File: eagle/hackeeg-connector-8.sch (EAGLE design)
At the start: 19 parts

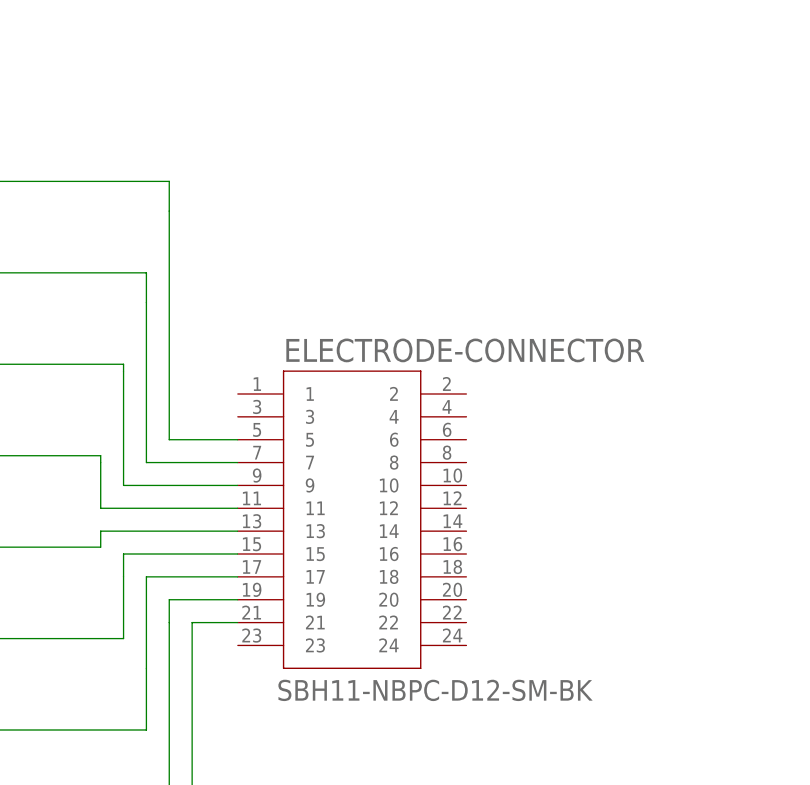
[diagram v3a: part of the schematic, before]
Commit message: connected IN1-8N to AGND
- for cable noise reduction
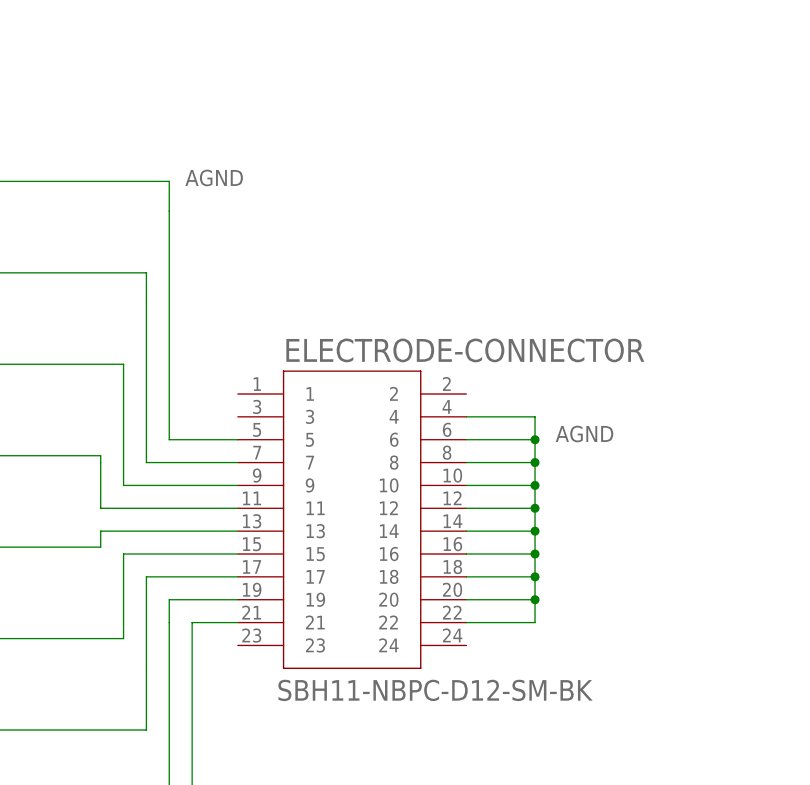
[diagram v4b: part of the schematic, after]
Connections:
- removed net N$1: AGND.SIGNAL, ELECTRODE-CONNECTOR.5
- new net AGND: AGND.SIGNAL, ELECTRODE-CONNECTOR.10, ELECTRODE-CONNECTOR.12, ELECTRODE-CONNECTOR.14, ELECTRODE-CONNECTOR.16, ELECTRODE-CONNECTOR.18, ELECTRODE-CONNECTOR.20, ELECTRODE-CONNECTOR.22, ELECTRODE-CONNECTOR.4, ELECTRODE-CONNECTOR.5, ELECTRODE-CONNECTOR.6, ELECTRODE-CONNECTOR.8
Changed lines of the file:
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@@
 </busses>
 <nets>
-<net name="N$1" class="0">
-<segment>
-<pinref part="AGND" gate="G$1" pin="SIGNAL"/>
-<wire x1="238.506" y1="191.262" x2="271.78" y2="191.262" width="0.1524" layer="91"/>
-<wire x1="271.78" y1="191.262" x2="271.78" y2="187.96" width="0.1524" layer="91"/>
-<pinref part="ELECTRODE-CONNECTOR" gate="G$1" pin="5"/>
-<wire x1="271.78" y1="187.96" x2="271.78" y2="162.56" width="0.1524" layer="91"/>
-<wire x1="271.78" y1="162.56" x2="279.4" y2="162.56" width="0.1524" layer="91"/>
-</segment>
-</net>
 <net name="N$2" class="0">
 <segment>
@@
 </segment>
 </net>
+<net name="AGND" class="0">
+<segment>
+<pinref part="ELECTRODE-CONNECTOR" gate="G$1" pin="4"/>
+<wire x1="304.8" y1="165.1" x2="312.42" y2="165.1" width="0.1524" layer="91"/>
+<wire x1="312.42" y1="165.1" x2="312.42" y2="162.56" width="0.1524" layer="91"/>
+<wire x1="312.42" y1="162.56" x2="312.42" y2="160.02" width="0.1524" layer="91"/>
+<wire x1="312.42" y1="160.02" x2="312.42" y2="157.48" width="0.1524" layer="91"/>
+<wire x1="312.42" y1="157.48" x2="312.42" y2="154.94" width="0.1524" layer="91"/>
+<wire x1="312.42" y1="154.94" x2="312.42" y2="152.4" width="0.1524" layer="91"/>
+<wire x1="312.42" y1="152.4" x2="312.42" y2="149.86" width="0.1524" layer="91"/>
+<wire x1="312.42" y1="149.86" x2="312.42" y2="147.32" width="0.1524" layer="91"/>
+<wire x1="312.42" y1="147.32" x2="312.42" y2="144.78" width="0.1524" layer="91"/>
+<wire x1="312.42" y1="144.78" x2="312.42" y2="142.24" width="0.1524" layer="91"/>
+<pinref part="ELECTRODE-CONNECTOR" gate="G$1" pin="6"/>
+<wire x1="304.8" y1="162.56" x2="312.42" y2="162.56" width="0.1524" layer="91"/>
+<junction x="312.42" y="162.56"/>
+<pinref part="ELECTRODE-CONNECTOR" gate="G$1" pin="8"/>
+<wire x1="304.8" y1="160.02" x2="312.42" y2="160.02" width="0.1524" layer="91"/>
+<junction x="312.42" y="160.02"/>
+<pinref part="ELECTRODE-CONNECTOR" gate="G$1" pin="10"/>
+<wire x1="304.8" y1="157.48" x2="312.42" y2="157.48" width="0.1524" layer="91"/>
+<junction x="312.42" y="157.48"/>
+<pinref part="ELECTRODE-CONNECTOR" gate="G$1" pin="12"/>
+<wire x1="304.8" y1="154.94" x2="312.42" y2="154.94" width="0.1524" layer="91"/>
+<junction x="312.42" y="154.94"/>
+<pinref part="ELECTRODE-CONNECTOR" gate="G$1" pin="14"/>
+<wire x1="304.8" y1="152.4" x2="312.42" y2="152.4" width="0.1524" layer="91"/>
+<junction x="312.42" y="152.4"/>
+<pinref part="ELECTRODE-CONNECTOR" gate="G$1" pin="16"/>
+<wire x1="304.8" y1="149.86" x2="312.42" y2="149.86" width="0.1524" layer="91"/>
+<junction x="312.42" y="149.86"/>
+<pinref part="ELECTRODE-CONNECTOR" gate="G$1" pin="18"/>
+<wire x1="304.8" y1="147.32" x2="312.42" y2="147.32" width="0.1524" layer="91"/>
+<junction x="312.42" y="147.32"/>
+<pinref part="ELECTRODE-CONNECTOR" gate="G$1" pin="20"/>
+<wire x1="304.8" y1="144.78" x2="312.42" y2="144.78" width="0.1524" layer="91"/>
+<junction x="312.42" y="144.78"/>
+<pinref part="ELECTRODE-CONNECTOR" gate="G$1" pin="22"/>
+<wire x1="304.8" y1="142.24" x2="312.42" y2="142.24" width="0.1524" layer="91"/>
+<label x="314.706" y="162.306" size="1.778" layer="95"/>
+</segment>
+<segment>
+<pinref part="AGND" gate="G$1" pin="SIGNAL"/>
+<wire x1="238.506" y1="191.262" x2="271.78" y2="191.262" width="0.1524" layer="91"/>
+<wire x1="271.78" y1="191.262" x2="271.78" y2="187.96" width="0.1524" layer="91"/>
+<pinref part="ELECTRODE-CONNECTOR" gate="G$1" pin="5"/>
+<wire x1="271.78" y1="187.96" x2="271.78" y2="162.56" width="0.1524" layer="91"/>
+<wire x1="271.78" y1="162.56" x2="279.4" y2="162.56" width="0.1524" layer="91"/>
+<label x="273.558" y="190.754" size="1.778" layer="95"/>
+</segment>
+</net>

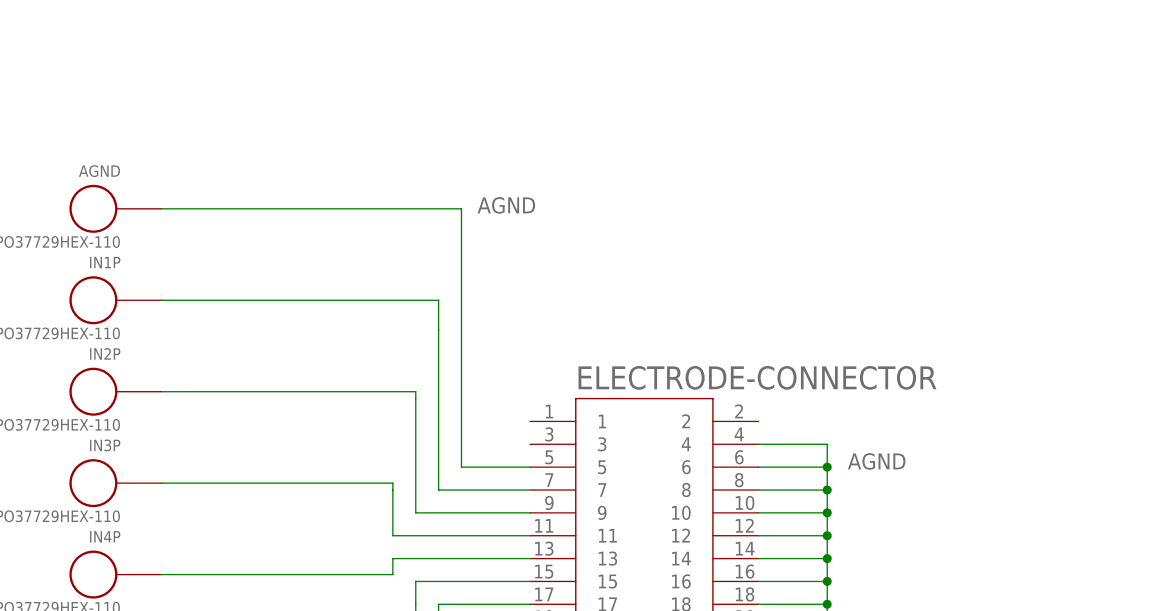
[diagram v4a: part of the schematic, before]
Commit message: reroute board with electrode conn on top
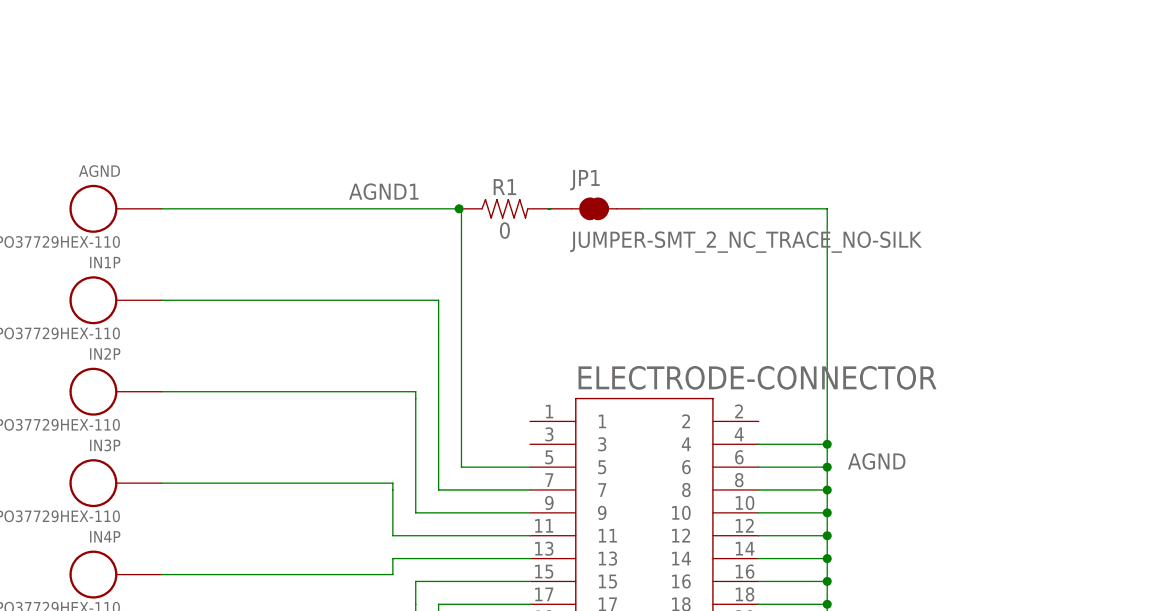
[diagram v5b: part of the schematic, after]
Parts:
- added JP1: JUMPER-SMT_2_NC_TRACE_NO-SILK, SparkFun-Jumpers:JUMPER-SMT_2_NC_TRACE_NO-SILK
- added R1: 0, SparkFun-Resistors:0OHM-0603-1/10W-5%
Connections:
- new net AGND1: AGND.SIGNAL, ELECTRODE-CONNECTOR.5, R1.1
- new net N$17: JP1.1, R1.2
- net AGND: now also JP1.2; no longer AGND.SIGNAL, ELECTRODE-CONNECTOR.5
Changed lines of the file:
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@@
 <part name="FD5" library="SparkFun-Aesthetics" library_urn="urn:adsk.eagle:library:507" deviceset="FIDUCIAL" device="1X2" package3d_urn="urn:adsk.eagle:package:37108/1"/>
 <part name="FD6" library="SparkFun-Aesthetics" library_urn="urn:adsk.eagle:library:507" deviceset="FIDUCIAL" device="1X2" package3d_urn="urn:adsk.eagle:package:37108/1"/>
+<part name="R1" library="SparkFun-Resistors" library_urn="urn:adsk.eagle:library:532" deviceset="0OHM" device="-0603-1/10W-5%" package3d_urn="urn:adsk.eagle:package:39650/1" value="0"/>
+<part name="JP1" library="SparkFun-Jumpers" library_urn="urn:adsk.eagle:library:528" deviceset="JUMPER-SMT_2_NC_TRACE" device="_NO-SILK" package3d_urn="urn:adsk.eagle:package:39286/1"/>
 </parts>
 <sheets>
@@
 <instance part="FD5" gate="G$1" x="355.6" y="132.08"/>
 <instance part="FD6" gate="G$1" x="355.6" y="119.38"/>
+<instance part="R1" gate="G$1" x="276.606" y="191.262"/>
+<instance part="JP1" gate="G$1" x="286.512" y="191.262"/>
 </instances>
 <busses>
@@
 <wire x1="304.8" y1="142.24" x2="312.42" y2="142.24" width="0.1524" layer="91"/>
 <label x="314.706" y="162.306" size="1.778" layer="95"/>
+<pinref part="JP1" gate="G$1" pin="2"/>
+<wire x1="291.592" y1="191.262" x2="312.42" y2="191.262" width="0.1524" layer="91"/>
+<wire x1="312.42" y1="191.262" x2="312.42" y2="165.1" width="0.1524" layer="91"/>
+<junction x="312.42" y="165.1"/>
 </segment>
+</net>
+<net name="AGND1" class="0">
 <segment>
 <pinref part="AGND" gate="G$1" pin="SIGNAL"/>
-<wire x1="238.506" y1="191.262" x2="271.78" y2="191.262" width="0.1524" layer="91"/>
+<wire x1="238.506" y1="191.262" x2="271.526" y2="191.262" width="0.1524" layer="91"/>
+<wire x1="271.526" y1="191.262" x2="271.78" y2="191.262" width="0.1524" layer="91"/>
 <wire x1="271.78" y1="191.262" x2="271.78" y2="187.96" width="0.1524" layer="91"/>
 <pinref part="ELECTRODE-CONNECTOR" gate="G$1" pin="5"/>
 <wire x1="271.78" y1="187.96" x2="271.78" y2="162.56" width="0.1524" layer="91"/>
 <wire x1="271.78" y1="162.56" x2="279.4" y2="162.56" width="0.1524" layer="91"/>
-<label x="273.558" y="190.754" size="1.778" layer="95"/>
+<label x="267.208" y="194.056" size="1.778" layer="95" rot="R180"/>
+<pinref part="R1" gate="G$1" pin="1"/>
+<junction x="271.526" y="191.262"/>
 </segment>
 </net>
+<net name="N$17" class="0">
+<segment>
+<pinref part="R1" gate="G$1" pin="2"/>
+<pinref part="JP1" gate="G$1" pin="1"/>
+<wire x1="281.686" y1="191.262" x2="281.432" y2="191.262" width="0.1524" layer="91"/>
+</segment>
+</net>

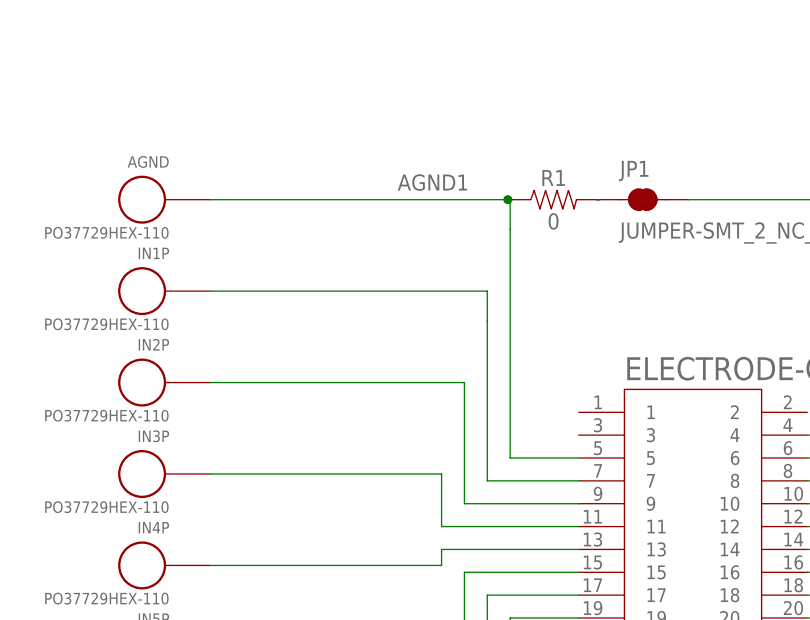
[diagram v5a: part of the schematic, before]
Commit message: connector-8 as sent to macrofab initial run
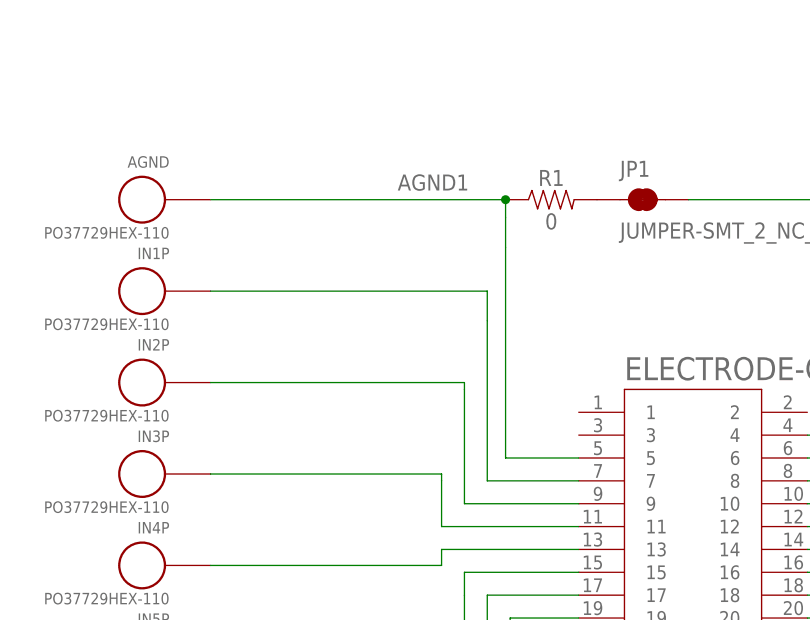
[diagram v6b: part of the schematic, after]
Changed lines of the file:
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@@
 <instance part="FD5" gate="G$1" x="355.6" y="132.08"/>
 <instance part="FD6" gate="G$1" x="355.6" y="119.38"/>
-<instance part="R1" gate="G$1" x="276.606" y="191.262"/>
+<instance part="R1" gate="G$1" x="276.352" y="191.262"/>
 <instance part="JP1" gate="G$1" x="286.512" y="191.262"/>
 </instances>
@@
 <segment>
 <pinref part="AGND" gate="G$1" pin="SIGNAL"/>
-<wire x1="238.506" y1="191.262" x2="271.526" y2="191.262" width="0.1524" layer="91"/>
-<wire x1="271.526" y1="191.262" x2="271.78" y2="191.262" width="0.1524" layer="91"/>
-<wire x1="271.78" y1="191.262" x2="271.78" y2="187.96" width="0.1524" layer="91"/>
+<wire x1="238.506" y1="191.262" x2="271.272" y2="191.262" width="0.1524" layer="91"/>
+<wire x1="271.272" y1="191.262" x2="271.272" y2="189.23" width="0.1524" layer="91"/>
+<wire x1="271.272" y1="189.23" x2="271.272" y2="185.928" width="0.1524" layer="91"/>
 <pinref part="ELECTRODE-CONNECTOR" gate="G$1" pin="5"/>
-<wire x1="271.78" y1="187.96" x2="271.78" y2="162.56" width="0.1524" layer="91"/>
-<wire x1="271.78" y1="162.56" x2="279.4" y2="162.56" width="0.1524" layer="91"/>
+<wire x1="271.272" y1="185.928" x2="271.272" y2="162.56" width="0.1524" layer="91"/>
+<wire x1="271.272" y1="162.56" x2="279.4" y2="162.56" width="0.1524" layer="91"/>
 <label x="267.208" y="194.056" size="1.778" layer="95" rot="R180"/>
 <pinref part="R1" gate="G$1" pin="1"/>
-<junction x="271.526" y="191.262"/>
+<junction x="271.272" y="191.262"/>
 </segment>
 </net>
@@
 <pinref part="R1" gate="G$1" pin="2"/>
 <pinref part="JP1" gate="G$1" pin="1"/>
-<wire x1="281.686" y1="191.262" x2="281.432" y2="191.262" width="0.1524" layer="91"/>
 </segment>
 </net>

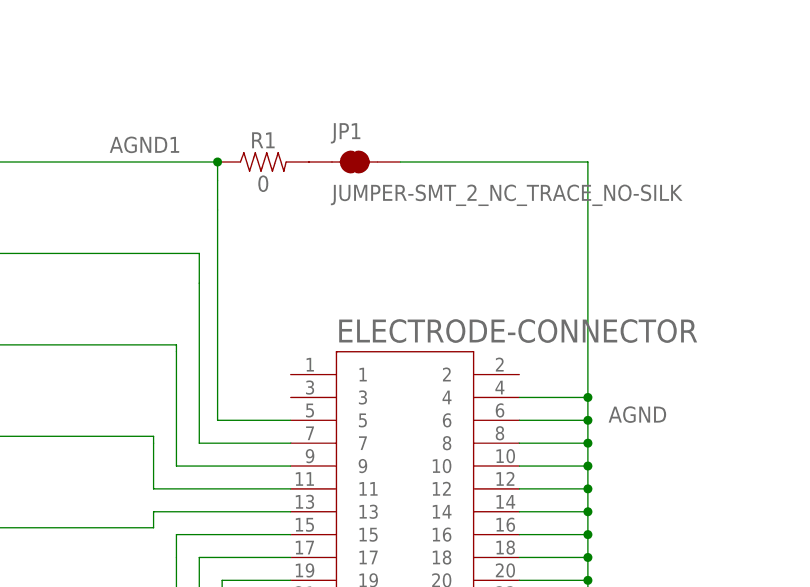
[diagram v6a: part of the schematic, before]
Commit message: corrected connector spacing and made board smaller
- all connectors are now evenly spaced
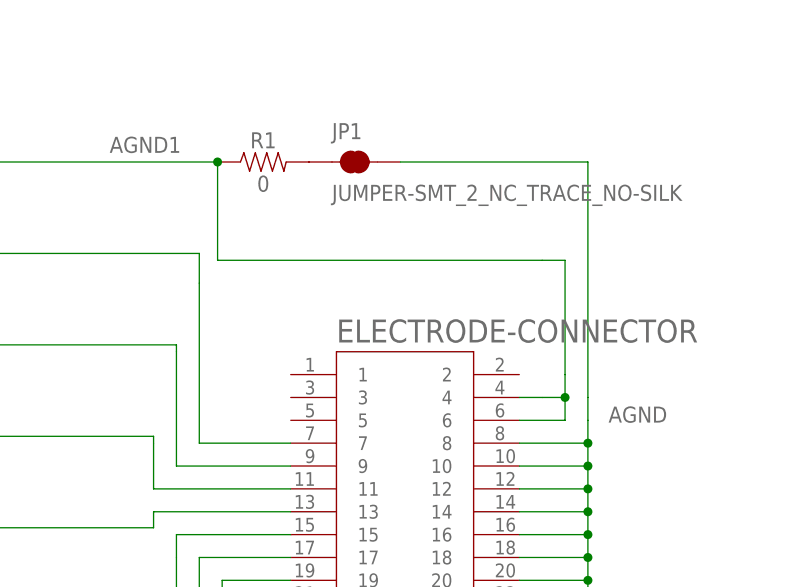
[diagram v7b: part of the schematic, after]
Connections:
- net AGND: no longer ELECTRODE-CONNECTOR.4, ELECTRODE-CONNECTOR.6
- net AGND1: now also ELECTRODE-CONNECTOR.4, ELECTRODE-CONNECTOR.6; no longer ELECTRODE-CONNECTOR.5
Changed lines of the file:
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@@
 <net name="AGND" class="0">
 <segment>
-<pinref part="ELECTRODE-CONNECTOR" gate="G$1" pin="4"/>
-<wire x1="304.8" y1="165.1" x2="312.42" y2="165.1" width="0.1524" layer="91"/>
 <wire x1="312.42" y1="165.1" x2="312.42" y2="162.56" width="0.1524" layer="91"/>
 <wire x1="312.42" y1="162.56" x2="312.42" y2="160.02" width="0.1524" layer="91"/>
@@
 <wire x1="312.42" y1="147.32" x2="312.42" y2="144.78" width="0.1524" layer="91"/>
 <wire x1="312.42" y1="144.78" x2="312.42" y2="142.24" width="0.1524" layer="91"/>
-<pinref part="ELECTRODE-CONNECTOR" gate="G$1" pin="6"/>
-<wire x1="304.8" y1="162.56" x2="312.42" y2="162.56" width="0.1524" layer="91"/>
-<junction x="312.42" y="162.56"/>
 <pinref part="ELECTRODE-CONNECTOR" gate="G$1" pin="8"/>
 <wire x1="304.8" y1="160.02" x2="312.42" y2="160.02" width="0.1524" layer="91"/>
@@
 <wire x1="291.592" y1="191.262" x2="312.42" y2="191.262" width="0.1524" layer="91"/>
 <wire x1="312.42" y1="191.262" x2="312.42" y2="165.1" width="0.1524" layer="91"/>
-<junction x="312.42" y="165.1"/>
 </segment>
 </net>
@@
 <pinref part="AGND" gate="G$1" pin="SIGNAL"/>
 <wire x1="238.506" y1="191.262" x2="271.272" y2="191.262" width="0.1524" layer="91"/>
-<wire x1="271.272" y1="191.262" x2="271.272" y2="189.23" width="0.1524" layer="91"/>
-<wire x1="271.272" y1="189.23" x2="271.272" y2="185.928" width="0.1524" layer="91"/>
-<pinref part="ELECTRODE-CONNECTOR" gate="G$1" pin="5"/>
-<wire x1="271.272" y1="185.928" x2="271.272" y2="162.56" width="0.1524" layer="91"/>
-<wire x1="271.272" y1="162.56" x2="279.4" y2="162.56" width="0.1524" layer="91"/>
 <label x="267.208" y="194.056" size="1.778" layer="95" rot="R180"/>
 <pinref part="R1" gate="G$1" pin="1"/>
+<wire x1="271.272" y1="191.262" x2="271.272" y2="180.34" width="0.1524" layer="91"/>
+<wire x1="271.272" y1="180.34" x2="307.34" y2="180.34" width="0.1524" layer="91"/>
 <junction x="271.272" y="191.262"/>
+<wire x1="307.34" y1="180.34" x2="309.88" y2="180.34" width="0.1524" layer="91"/>
+<wire x1="309.88" y1="180.34" x2="309.88" y2="167.64" width="0.1524" layer="91"/>
+<pinref part="ELECTRODE-CONNECTOR" gate="G$1" pin="4"/>
+<wire x1="304.8" y1="165.1" x2="307.34" y2="165.1" width="0.1524" layer="91"/>
+<wire x1="307.34" y1="165.1" x2="309.88" y2="165.1" width="0.1524" layer="91"/>
+<wire x1="309.88" y1="165.1" x2="309.88" y2="167.64" width="0.1524" layer="91"/>
+<pinref part="ELECTRODE-CONNECTOR" gate="G$1" pin="6"/>
+<wire x1="304.8" y1="162.56" x2="309.88" y2="162.56" width="0.1524" layer="91"/>
+<wire x1="309.88" y1="162.56" x2="309.88" y2="165.1" width="0.1524" layer="91"/>
+<junction x="309.88" y="165.1"/>
 </segment>
 </net>
